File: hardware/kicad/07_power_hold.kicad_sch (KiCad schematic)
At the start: 0 parts

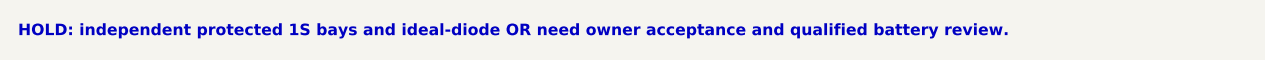
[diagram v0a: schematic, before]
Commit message: docs: accept GNSS and removable 2S direction
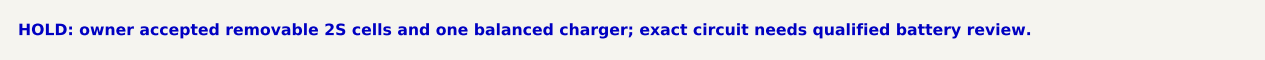
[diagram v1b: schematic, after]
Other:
- note added: "HOLD: owner accepted removable 2S cells and one balanced charger; exact circuit needs qualified battery review."
- note removed: "HOLD: independent protected 1S bays and ideal-diode OR need owner acceptance and qualified battery review."
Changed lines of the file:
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@@
 	(paper "A4")
 	(title_block (title "07 Power - HOLD") (rev "architecture-gate"))
-	(text "HOLD: independent protected 1S bays and ideal-diode OR need owner acceptance and qualified battery review." (exclude_from_sim no) (at 25.4 30.48 0) (effects (font (size 1.27 1.27) (bold yes)) (justify left bottom)))
+	(text "HOLD: owner accepted removable 2S cells and one balanced charger; exact circuit needs qualified battery review." (exclude_from_sim no) (at 25.4 30.48 0) (effects (font (size 1.27 1.27) (bold yes)) (justify left bottom)))
 	(sheet_instances (path "/" (page "1")))
 	(embedded_fonts no)
